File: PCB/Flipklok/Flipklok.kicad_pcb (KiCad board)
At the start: 2 copper layers, 48 x 72 mm, 70 parts, among them J1 Power, J10 FW-btn, J11 EX-btn, J12 Programheader, J2 SW, J3 28BYJ-48, J4 Backlight, J5 DCF77, J6 LDR, J8 Indicator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

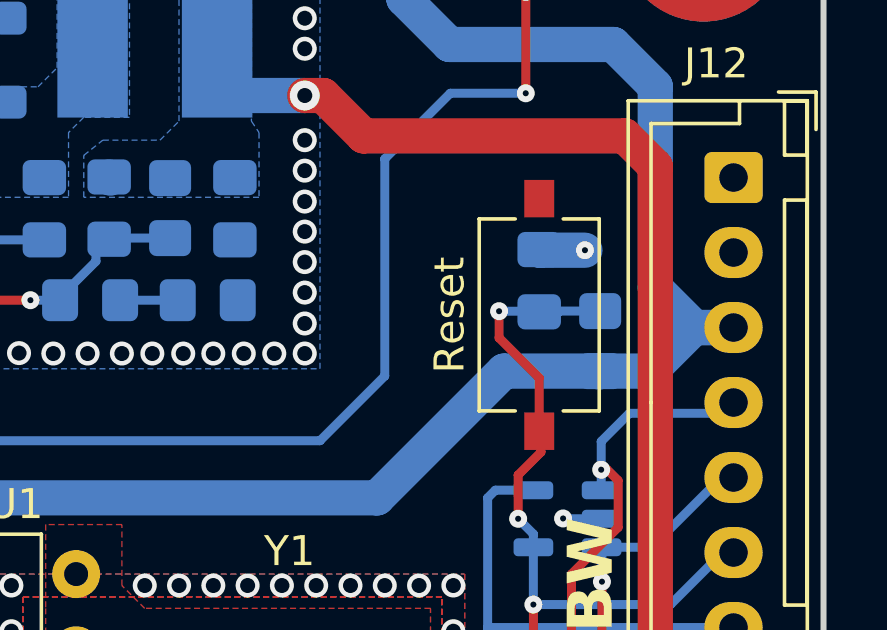
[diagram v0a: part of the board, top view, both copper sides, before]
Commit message: filled in "to be detriment values" and updated BOM
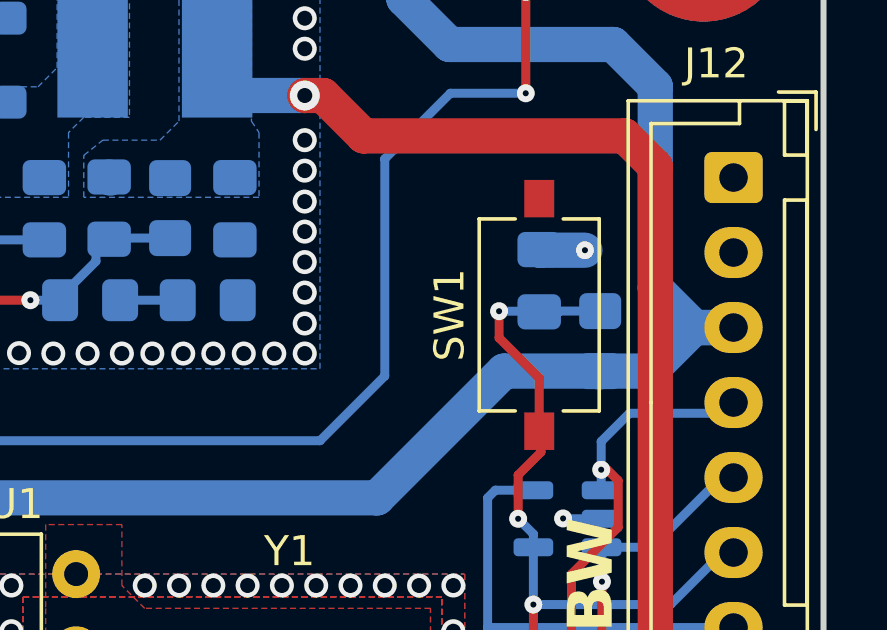
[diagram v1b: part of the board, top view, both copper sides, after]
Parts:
- C14: value C -> 100n
- R14: value R -> 10k
- R4, R6: value R -> 75k
- R5, R7: value R -> 18k
- renumbered Reset to SW1

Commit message: filled in led resistor
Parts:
- R13: value R -> 470
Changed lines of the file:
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@@
 		(sheetname "/")
 		(sheetfile "Flipklok.kicad_sch")
-		(attr smd dnp)
+		(attr smd exclude_from_bom dnp)
 		(fp_line
 			(start -0.227064 -0.735)
@@
 		(sheetname "/")
 		(sheetfile "Flipklok.kicad_sch")
-		(attr smd dnp)
+		(attr smd exclude_from_bom dnp)
 		(fp_line
 			(start -0.261252 -0.735)
@@
 		(sheetname "/")
 		(sheetfile "Flipklok.kicad_sch")
-		(attr smd dnp)
+		(attr smd exclude_from_bom dnp)
 		(fp_line
 			(start -0.261252 -0.735)
@@
 			)
 		)
-		(property "Value" "R"
+		(property "Value" "470"
 			(at 0 -1.65 0)
 			(layer "B.Fab")
